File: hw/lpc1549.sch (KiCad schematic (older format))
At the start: 17 parts, among them J201 ARM_JTAG_SWD_HEADER_10_PINSMD, U201 LPC1549JBD64, U202 MCP2551_SOIC8, X201 XTAL_7A-12.000MAAJ-T

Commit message: starting to draw version 4.0.0
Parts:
- renumbered C201 to C1301, C202 to C1302, C203 to C1303, C204 to C1304, C205 to C1305, C206 to C1306, C207 to C1307, C208 to C1308, C209 to C1309, J201 to J1301, R201 to R1301, R202 to R1302, R203 to R1303, R204 to R1304, U201 to U1301, U202 to U1302, X201 to X1301
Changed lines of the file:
@@
 $EndDescr
 $Comp
-L 100nF C206
+L 100nF C1306
 U 1 1 57E685B4
 P 4400 4100
-F 0 "C206" V 4408 4173 45  0000 L CNN
+F 0 "C1306" V 4408 4173 45  0000 L CNN
 F 1 "100nF" V 4492 4173 45  0000 L CNN
 F 2 "kemet:0603" H 4430 4250 20  0001 C CNN
@@
 $EndComp
 $Comp
-L 100nF C205
+L 100nF C1305
 U 1 1 57E68621
 P 4050 4100
-F 0 "C205" V 4058 4173 45  0000 L CNN
+F 0 "C1305" V 4058 4173 45  0000 L CNN
 F 1 "100nF" V 4142 4173 45  0000 L CNN
 F 2 "kemet:0603" H 4080 4250 20  0001 C CNN
@@
 $EndComp
 $Comp
-L 100nF C204
+L 100nF C1304
 U 1 1 57E68672
 P 3700 4100
-F 0 "C204" V 3708 4173 45  0000 L CNN
+F 0 "C1304" V 3708 4173 45  0000 L CNN
 F 1 "100nF" V 3792 4173 45  0000 L CNN
 F 2 "kemet:0603" H 3730 4250 20  0001 C CNN
@@
 $EndComp
 $Comp
-L 100nF C203
+L 100nF C1303
 U 1 1 57E686C7
 P 3350 4100
-F 0 "C203" V 3358 4173 45  0000 L CNN
+F 0 "C1303" V 3358 4173 45  0000 L CNN
 F 1 "100nF" V 3442 4173 45  0000 L CNN
 F 2 "kemet:0603" H 3380 4250 20  0001 C CNN
@@
 $EndComp
 $Comp
-L 100nF C202
+L 100nF C1302
 U 1 1 57E6871C
 P 3000 4100
-F 0 "C202" V 3008 4173 45  0000 L CNN
+F 0 "C1302" V 3008 4173 45  0000 L CNN
 F 1 "100nF" V 3092 4173 45  0000 L CNN
 F 2 "kemet:0603" H 3030 4250 20  0001 C CNN
@@
 $EndComp
 $Comp
-L XTAL_7A-12.000MAAJ-T X201
+L XTAL_7A-12.000MAAJ-T X1301
 U 1 1 57E6956F
 P 6650 2850
-F 0 "X201" V 6558 2948 45  0000 L CNN
+F 0 "X1301" V 6558 2948 45  0000 L CNN
 F 1 "XTAL_7A-12.000MAAJ-T" V 6850 2700 45  0000 L CNN
 F 2 "usevolt:XTAL_7A-20.000MAJ" H 6680 3000 20  0001 C CNN
@@
 $EndComp
 $Comp
-L 18pF C207
+L 18pF C1307
 U 1 1 57E695FA
 P 6950 2650
-F 0 "C207" H 6900 2600 45  0000 C CNN
+F 0 "C1307" H 6900 2600 45  0000 C CNN
 F 1 "18pF" H 7100 2600 45  0000 C CNN
 F 2 "kemet:0603" H 6980 2800 20  0001 C CNN
@@
 $EndComp
 $Comp
-L 18pF C208
+L 18pF C1308
 U 1 1 57E69648
 P 6950 2950
-F 0 "C208" H 6900 3000 45  0000 C CNN
+F 0 "C1308" H 6900 3000 45  0000 C CNN
 F 1 "18pF" H 7100 3000 45  0000 C CNN
 F 2 "kemet:0603" H 6980 3100 20  0001 C CNN
@@
 RESET
 $Comp
-L 10K R203
+L 10K R1303
 U 1 1 589226EB
 P 8150 3550
-F 0 "R203" V 8158 3608 45  0000 L CNN
+F 0 "R1303" V 8158 3608 45  0000 L CNN
 F 1 "10K" V 8242 3608 45  0000 L CNN
 F 2 "multicomp:0603" H 8180 3700 20  0001 C CNN
@@
 $EndComp
 $Comp
-L 10K R204
+L 10K R1304
 U 1 1 58922760
 P 8400 3600
-F 0 "R204" V 8408 3658 45  0000 L CNN
+F 0 "R1304" V 8408 3658 45  0000 L CNN
 F 1 "10K" V 8492 3658 45  0000 L CNN
 F 2 "multicomp:0603" H 8430 3750 20  0001 C CNN
@@
 AR Path="/58C01592" Ref="C?"  Part="1"
 AR Path="/57E682A9/58C01592" Ref="C?"  Part="1"
-AR Path="/5953E91C/58C01592" Ref="C209"  Part="1"
-F 0 "C209" V 10208 5873 45  0000 L CNN
+AR Path="/5953E91C/58C01592" Ref="C1309"  Part="1"
+F 0 "C1309" V 10208 5873 45  0000 L CNN
 F 1 "100nF" V 10292 5873 45  0000 L CNN
 F 2 "kemet:0603" H 10230 5950 20  0001 C CNN
@@
 	9550 5250 8650 5250
 $Comp
-L 100nF C201
+L 100nF C1301
 U 1 1 58D0A5A6
 P 2650 4100
-F 0 "C201" V 2658 4173 45  0000 L CNN
+F 0 "C1301" V 2658 4173 45  0000 L CNN
 F 1 "100nF" V 2742 4173 45  0000 L CNN
 F 2 "kemet:0603" H 2680 4250 20  0001 C CNN
@@
 Connection ~ 3000 4000
 $Comp
-L LPC1549JBD64 U201
+L LPC1549JBD64 U1301
 U 1 1 5946DE63
 P 5100 2650
-F 0 "U201" H 5500 3726 45  0000 C CNN
+F 0 "U1301" H 5500 3726 45  0000 C CNN
 F 1 "LPC1549JBD64" H 5100 2650 45  0001 L BNN
 F 2 "usevolt:QFP64" H 5130 2800 20  0001 C CNN
@@
 Connection ~ 4400 4300
 $Comp
-L ARM_JTAG_SWD_HEADER_10_PINSMD J201
+L ARM_JTAG_SWD_HEADER_10_PINSMD J1301
 U 1 1 5953ECE3
 P 8850 3950
-F 0 "J201" H 9377 3892 45  0000 L CNN
+F 0 "J1301" H 9377 3892 45  0000 L CNN
 F 1 "ARM_JTAG_SWD_HEADER_10_PINSMD" H 9377 3808 45  0000 L CNN
 F 2 "usevolt:ARM_10_PIN_JTAG_SWD_CONNECTOR" H 8880 4100 20  0001 C CNN
@@
 $EndComp
 $Comp
-L MCP2551_SOIC8 U202
+L MCP2551_SOIC8 U1302
 U 1 1 5953EADD
 P 9300 5800
-F 0 "U202" H 9350 6104 45  0000 C CNN
+F 0 "U1302" H 9350 6104 45  0000 C CNN
 F 1 "MCP2551_SOIC8" H 9350 6020 45  0000 C CNN
 F 2 "usevolt:SOIC8" H 9180 5950 20  0001 C CNN
@@
 Connection ~ 9750 6000
 $Comp
-L 10K R201
+L 10K R1301
 U 1 1 5957A035
 P 6600 2450
-F 0 "R201" H 6650 2634 45  0000 C CNN
+F 0 "R1301" H 6650 2634 45  0000 C CNN
 F 1 "10K" H 6650 2550 45  0000 C CNN
 F 2 "multicomp:0603" H 6630 2600 20  0001 C CNN
@@
 WIPER_POS
 $Comp
-L 10K R202
+L 10K R1302
 U 1 1 5957B1E8
 P 6850 2550
-F 0 "R202" H 6900 2734 45  0000 C CNN
+F 0 "R1302" H 6900 2734 45  0000 C CNN
 F 1 "10K" H 6900 2650 45  0000 C CNN
 F 2 "multicomp:0603" H 6880 2700 20  0001 C CNN

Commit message: 3.1.0 hw created, not yet ordered
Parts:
- removed U1301: LPC1549JBD64, usevolt:QFP64, symbol LPC1549JBD64
- removed U1302: MCP2551_SOIC8, usevolt:SOIC8, symbol MCP2551_SOIC8
- added U301: LPC1549JBD64, usevolt:QFP64, symbol LPC1549JBD64
- added U302: MCP2551_SOIC8, usevolt:SOIC8, symbol MCP2551_SOIC8
- renumbered C1301 to C301, C1302 to C302, C1303 to C303, C1304 to C304, C1305 to C305, C1306 to C306, C1307 to C307, C1308 to C308, C1309 to C309, J1301 to J301, R1301 to R301, R1302 to R302, R1303 to R303, R1304 to R304, X1301 to X301
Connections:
- net +3V3: now also U301.P$13 (VREF_ADC), U301.P$18 (VREFP_DAC_VDDCMP), U301.P$20 (VDDA), U301.P$22 (VDD), U301.P$37 (VDD), U301.P$52 (VDD), U301.P$57 (VDD)
- net +5V: now also U302.3 (VDD)
- net BACK: now also U301.P$7 (PIO0_3/ADC0_5/SCT1_OUT4)
- net BACK_SENSE: now also U301.P$6 (PIO0_2/ADC0_6/SCT1_OUT3)
- net BEACON: now also U301.P$8 (PIO0_4/ADC0_4)
- net BEACON_SENSE: now also U301.P$5 (PIO0_1/ADC0_7/SCT0_OUT4)
- net CANH: now also U302.7 (CANH)
- net CANL: now also U302.6 (CANL)
- net CAN_RX: now also U301.P$59 (PIO1_10/CAN_RX), U302.4 (RXD)
- net CAN_TX: now also U301.P$60 (PIO0_25/CAN_TX), U302.1 (TXD)
- net COOLER: now also U301.P$29 (PIO0_13/ADC1_6)
- net COOLER_SENSE: now also U301.P$30 (PIO0_14/ADC1_7/SCT1_OUT5)
- net DRIVE: now also U301.P$11 (PIO0_7/ADC0_1)
- net DRIVE_SENSE: now also U301.P$12 (PIO0_8/ADC0_0/TDO)
- net GND: now also U301.P$14 (VREFN), U301.P$21 (VSSA), U301.P$26 (VSS), U301.P$27 (VSS), U301.P$41 (VBAT), U301.P$55 (VSS), U301.P$56 (VSS), U302.2 (VSS), U302.8 (RS/GND)
- net IN: now also U301.P$3 (PIO0_31/ADC0_9)
- net IN_SENSE: now also U301.P$2 (PIO0_0/ADC0_10/SCT0_OUT3)
- net OILCOOLER: now also U301.P$31 (PIO0_15/ADC1_8)
- net OILCOOLER_SENSE: now also U301.P$32 (PIO0_16/ADC1_9)
- net RESET: now also U301.P$45 (~RESET~/PIO0_21)
- net WIPER: now also U301.P$4 (PIO1_0/ADC0_8)
- net WIPER_SENSE: now also U301.P$1 (PIO0_30/ADC0_11)
- net WORK: now also U301.P$9 (PIO0_5/ADC0_3)
- net WORK_SENSE: now also U301.P$10 (PIO0_6/ADC0_2/SCT2_OUT3)
- net at C307.1 (C1), X301.P$1: now also U301.P$35 (XTALOUT)
- net at C308.1 (C1), X301.P$2: now also U301.P$36 (XTALIN)
- net at J301.P$2 (TMS/SWDIO), R303.1 (R1): now also U301.P$44 (SWDIO/PIO0_20/SCT1_OUT6/TMS)
- net at J301.P$4 (TCK/SWDCLK), R304.1 (R1): now also U301.P$40 (SWCLK/PIO0_19/TCK)
- net at R301.2 (R2): now also U301.P$33 (PIO1_4/ADC1_10)
- net at R302.2 (R2): now also U301.P$34 (PIO1_5/ADC1_11)
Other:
- moved on the sheet: J301, R303, R304

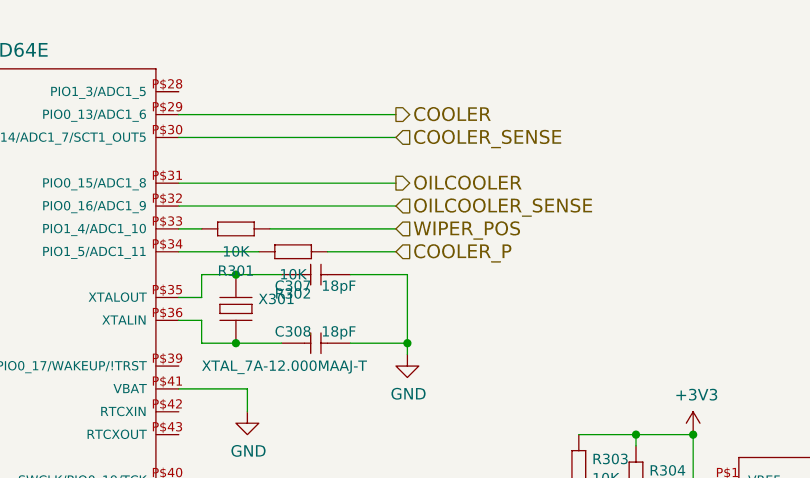
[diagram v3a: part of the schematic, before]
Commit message: oil cooler removed, 3.2.0 ready to order
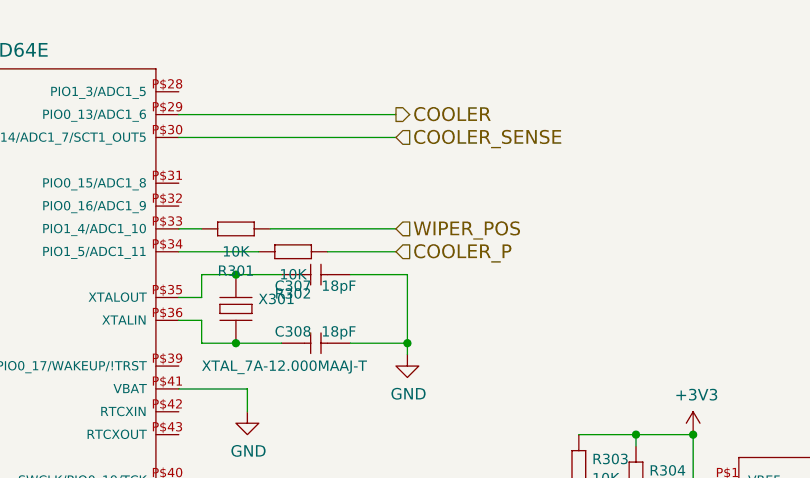
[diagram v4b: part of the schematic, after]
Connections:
- net OILCOOLER: no longer names the net of U301.P$31 (PIO0_15/ADC1_8)
- net OILCOOLER_SENSE: no longer names the net of U301.P$32 (PIO0_16/ADC1_9)
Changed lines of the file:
@@
 $Descr A4 11693 8268
 encoding utf-8
-Sheet 3 9
+Sheet 3 8
 Title ""
 Date ""
@@
 	10100 5600 10100 5700
 Connection ~ 10100 5700
-Wire Wire Line
-	6400 2350 7350 2350
-Text HLabel 7350 2350 2    60   Input ~ 0
-OILCOOLER_SENSE
-Wire Wire Line
-	6400 2250 7350 2250
-Text HLabel 7350 2250 2    60   Output ~ 0
-OILCOOLER
 $Comp
 L LPC1549JBD64 U301
